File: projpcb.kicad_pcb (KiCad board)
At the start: 2 copper layers, 42 parts, among them CON1 BARREL_JACK, CON2 BARREL_JACK, P1 CONN_01X02, P2 CONN_01X02, P3 CONN_02X05, P4 CONN_02X05, Q1 SFH3711, Q10 SFH3711, Q11 SFH3711, Q12 SFH3711, Q13 SFH3711, Q14 SFH3711, Q15 SFH3711, Q16 Q_NMOS_GSD, Q2 SFH3711, Q3 SFH3711, Q4 SFH3711, Q5 SFH3711, Q6 SFH3711, Q7 SFH3711, Q8 SFH3711, Q9 SFH3711, U1 Teensy_3.1, U2 LM358, U3 CD74HC4067, U4 CL520

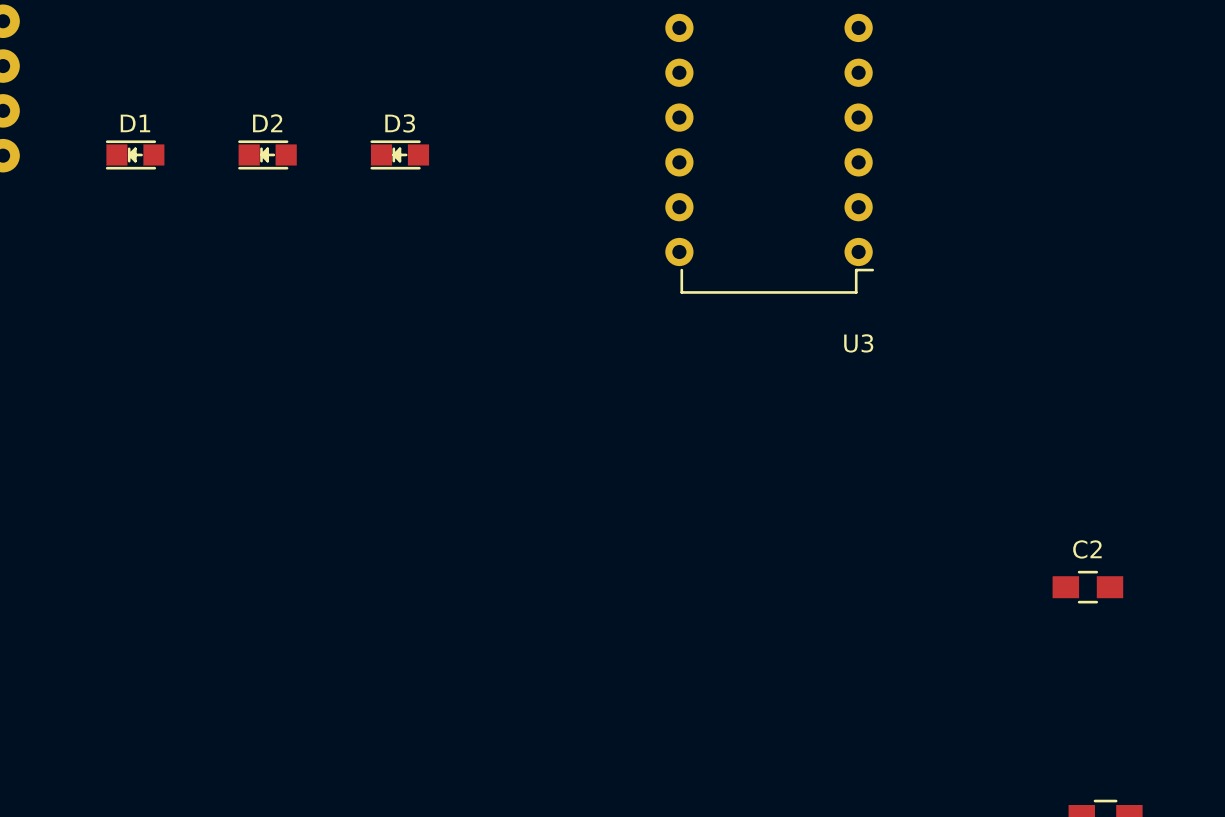
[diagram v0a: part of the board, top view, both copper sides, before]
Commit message: Changed VIN --> 3.3v, analog GND to AGND, added 3 status LED's
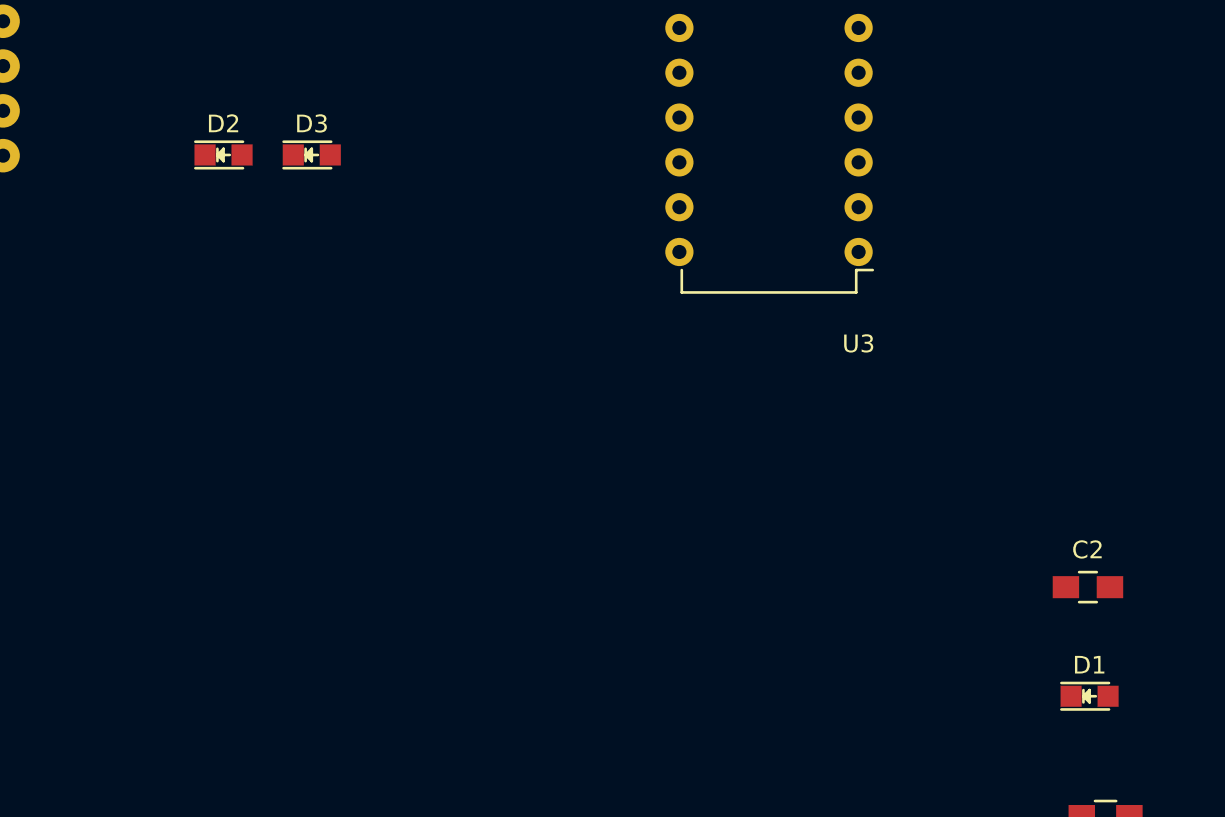
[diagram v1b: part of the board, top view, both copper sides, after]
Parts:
- moved D1 62.2 mm to (234.1, 148.2)
- moved D3 5.00 mm to (190.0, 117.5)
- moved D2 2.50 mm to (185.0, 117.5)
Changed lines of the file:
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@@
   )
   (module LEDs:LED_0805 (layer F.Cu)
-    (at 180 117.5)
+    (at 234.095001 148.185)
     (descr "LED 0805 smd package")
     (tags "LED 0805 SMD")
@@
   )
   (module LEDs:LED_0805 (layer F.Cu)
-    (at 187.5 117.5)
+    (at 185 117.5)
     (descr "LED 0805 smd package")
     (tags "LED 0805 SMD")
@@
   )
   (module LEDs:LED_0805 (layer F.Cu)
-    (at 195 117.5)
+    (at 190 117.5)
     (descr "LED 0805 smd package")
     (tags "LED 0805 SMD")

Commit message: PCB furtherererd
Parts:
- moved Q4 90.5 mm to (247.5, 70.0)
- moved R2 89.5 mm to (195.0, 110.0)
- moved Q6 87.4 mm to (232.5, 90.0)
- moved Q3 87.1 mm to (240.0, 90.0)
- moved Q5 86.5 mm to (240.0, 85.0)
- moved R5 86.5 mm to (195.0, 100.0)
- moved Q7 86.0 mm to (240.0, 80.0)
- moved C1 85.6 mm to (195.0, 105.0)
- moved Q2 80.9 mm to (260.0, 75.0)
- moved Q12 77.6 mm to (232.5, 85.0)
- moved Q1 77.3 mm to (260.0, 87.5)
- moved Q15 76.9 mm to (232.5, 80.0)
- moved Q14 76.1 mm to (232.5, 75.0)
- moved Q13 75.9 mm to (240.0, 75.0)
- moved Q9 72.0 mm to (240.0, 95.0)
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
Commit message: PCB
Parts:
- C2, P3, P4: moved to B.Cu
- moved Q16 64.3 mm to (152.4, 81.4), turned to 180 degrees
- moved U4 58.4 mm to (152.5, 105.0), turned to 90 degrees
- moved Q1 50.3 mm to (215.0, 65.0)
- moved Q10 50.2 mm to (225.0, 117.0)
- moved C2 48.8 mm to (158.6, 73.8), turned to 270 degrees
- moved Q4 47.0 mm to (215.0, 104.0)
- moved Q2 45.1 mm to (215.0, 78.0)
- moved R2 42.0 mm to (153.0, 110.8)
- moved Q5 40.6 mm to (215.0, 117.0)
- moved Q15 37.3 mm to (237.0, 117.0)
- moved R1 34.7 mm to (185.0, 77.5), turned to 180 degrees
- moved Q8 30.2 mm to (226.0, 91.0)
- moved Q14 29.3 mm to (237.0, 104.0)
- moved R3 29.2 mm to (177.5, 115.0)
- moved R4 28.0 mm to (185.0, 115.0), turned to 180 degrees
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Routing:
- net +3V3: track 0.00 -> 50.5 mm
- net Net-(RV1-Pad3): track 0.00 -> 40.2 mm
- net HEAT: track 0.00 -> 27.6 mm
- net TEMP_S: track 0.00 -> 14.9 mm
- net Net-(P2-Pad2): track 0.00 -> 5.53 mm
- net Net-(D3-Pad1): track 0.00 -> 2.54 mm
- net Net-(D2-Pad1): track 0.00 -> 2.54 mm
- net Net-(D1-Pad1): track 0.00 -> 2.54 mm

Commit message: PCB
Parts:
- removed P3, P4: CONN_02X05, Pin_Headers:Pin_Header_Straight_2x05
- R2, U3: moved to B.Cu
- moved Q1 52.0 mm to (215.0, 117.0)
- moved Q5 40.5 mm to (226.0, 78.0)
- moved U3 39.3 mm to (199.0, 71.8)
- moved RV2 29.6 mm to (151.9, 60.9), turned to 0 degrees
- moved Q8 28.2 mm to (215.0, 65.0)
- moved RV1 27.9 mm to (164.4, 61.2)
- moved Q2 26.0 mm to (215.0, 104.0)
- moved Q4 17.0 mm to (226.0, 91.0)
- moved Q6 17.0 mm to (215.0, 78.0), turned to 180 degrees
- moved R1 16.8 mm to (174.6, 64.3), turned to 270 degrees
- moved Q7 13.0 mm to (226.0, 65.0)
- moved R2 12.9 mm to (163.0, 119.0), turned to 180 degrees
- moved P1 5.00 mm to (142.5, 115.0)
- moved P2 5.00 mm to (142.5, 105.0)
- moved C1 3.75 mm to (195.0, 86.2), turned to 270 degrees
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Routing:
- net +3V3: track 50.5 -> 455.2 mm, vias 0 -> 2
- net /Phototransistors/S15: track 0.00 -> 162.2 mm
- net /Phototransistors/S14: track 0.00 -> 140.7 mm
- net /Phototransistors/S13: track 0.00 -> 120.3 mm
- net /Phototransistors/S12: track 0.00 -> 98.7 mm
- net /Phototransistors/S9: track 0.00 -> 83.0 mm
- net /Phototransistors/S10: track 0.00 -> 72.2 mm
- net /Phototransistors/S11: track 0.00 -> 69.2 mm
- net Net-(D3-Pad2): track 0.00 -> 63.7 mm
- net GNDA: track 0.00 -> 61.4 mm
- net Net-(D2-Pad2): track 0.00 -> 57.8 mm
- net Net-(RV2-Pad1): track 0.00 -> 53.3 mm
- net Net-(D1-Pad2): track 0.00 -> 50.1 mm
- net T2: track 0.00 -> 44.1 mm
- net Net-(CON2-Pad2): track 0.00 -> 34.0 mm
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- added copper zone on F.Cu, net GND
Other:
- board outline added: 110 x 72.5 mm
- net class HP added: clearance 0.2, trace_width 2, via_dia 0.6, via_drill 0.4
